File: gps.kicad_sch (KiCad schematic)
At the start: 17 parts, among them J700 Conn_01x02, U700 NEO-6P, X7 Conn_Coaxial

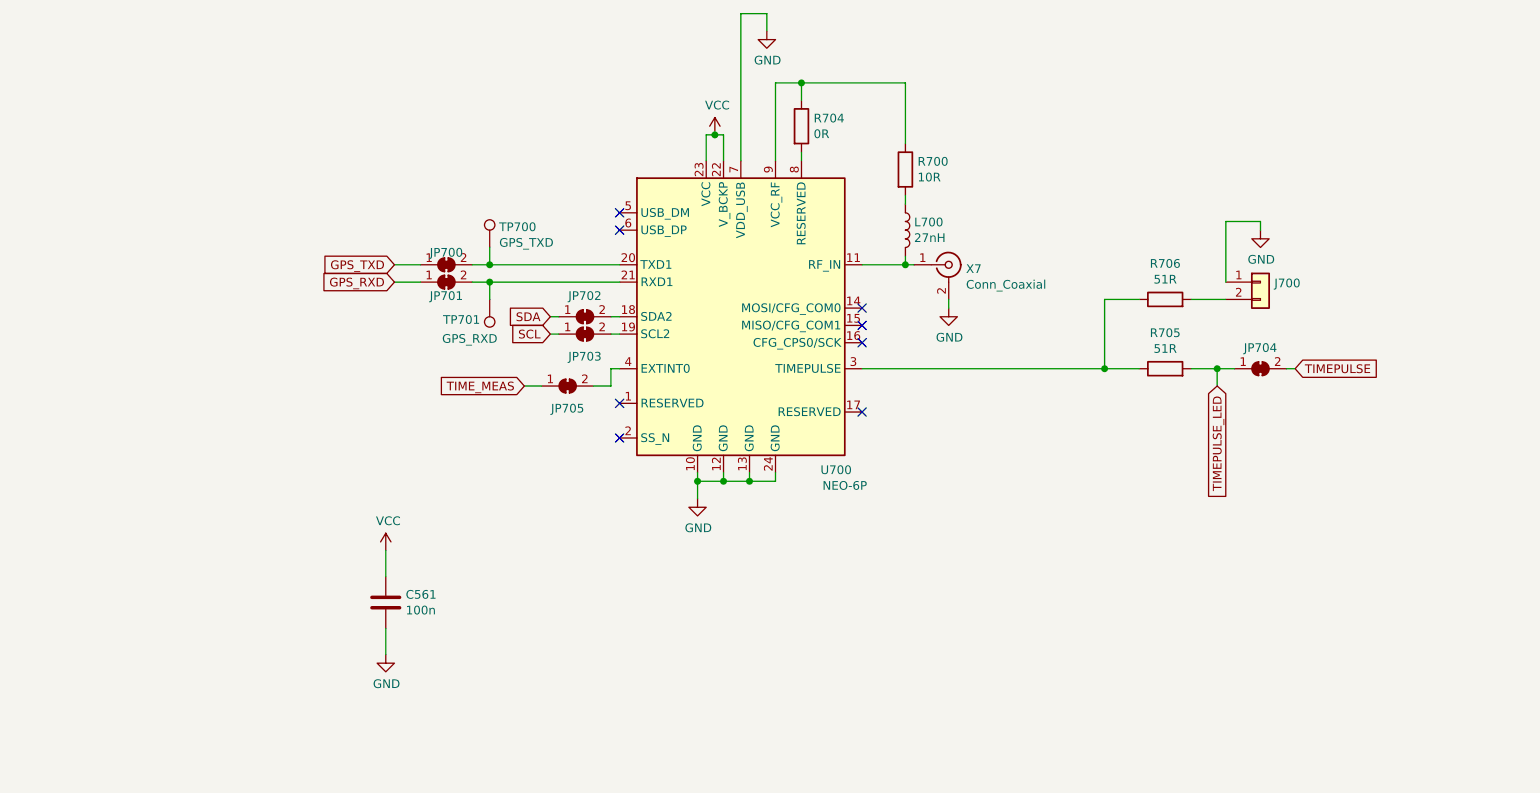
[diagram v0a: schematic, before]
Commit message: Refactored schematic to better show relationship in main schematic
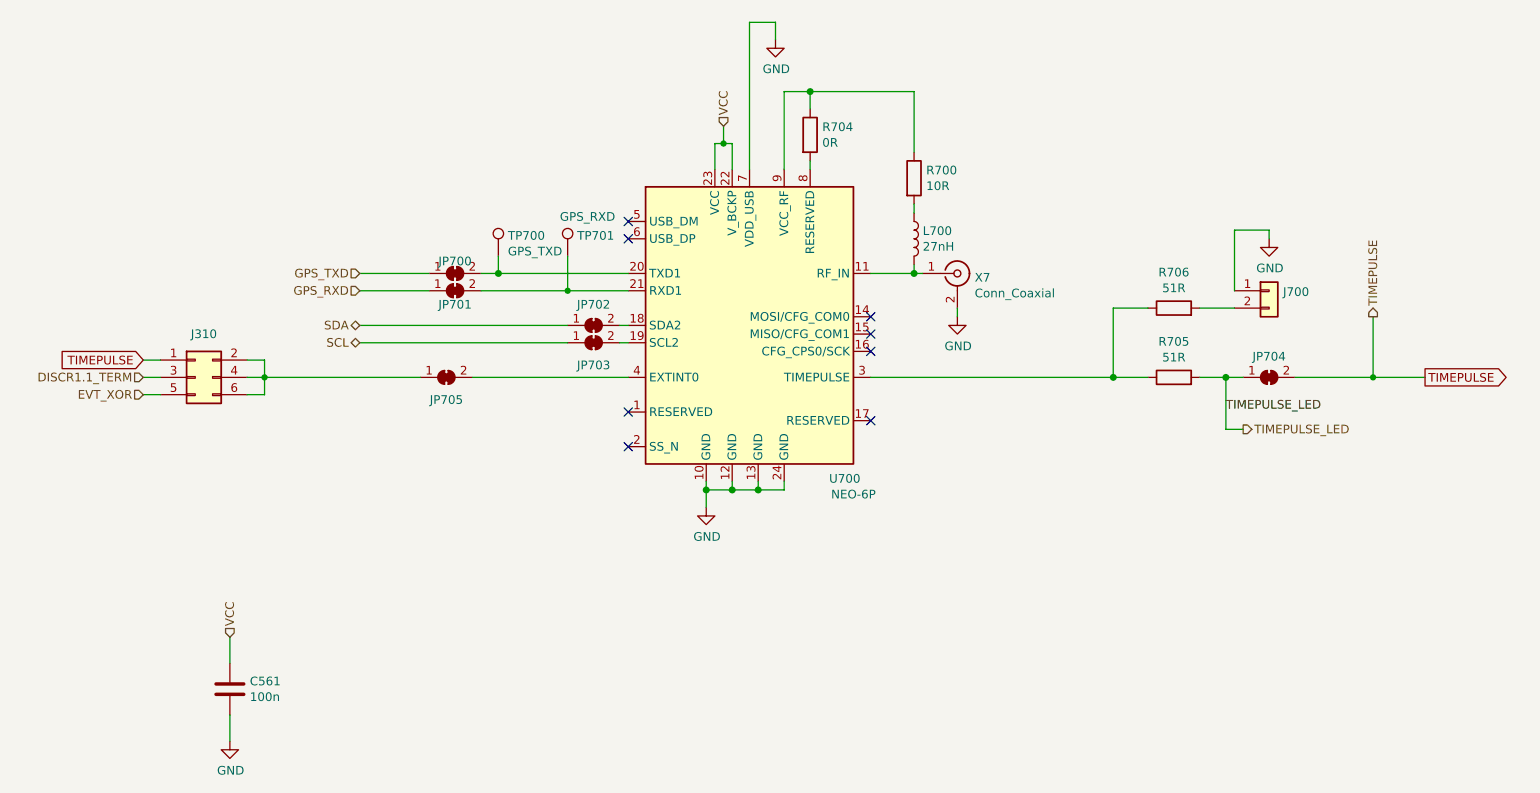
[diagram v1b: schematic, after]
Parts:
- added J310: Conn_02x03_Odd_Even, Connector_PinHeader_2.54mm:PinHeader_2x03_P2.54mm_Vertical, symbol Connector_Generic:Conn_02x03_Odd_Even
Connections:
- net TIMEPULSE: now also J310.1 (Pin_1)
- net TIME_MEAS: no longer names the net of JP705.1 (A)
- net TIME_MEAS: now also J310.2 (Pin_2), J310.4 (Pin_4), J310.6 (Pin_6)
- new net DISCR1.1_TERM: J310.3 (Pin_3)
- new net EVT_XOR: J310.5 (Pin_5)
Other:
- moved on the sheet: C561, J700, JP700, JP701, JP702, JP703, JP704, JP705, L700, R700, R704, R705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

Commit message: Cleaned up board, replaced GPIO footprint with unshrouded version
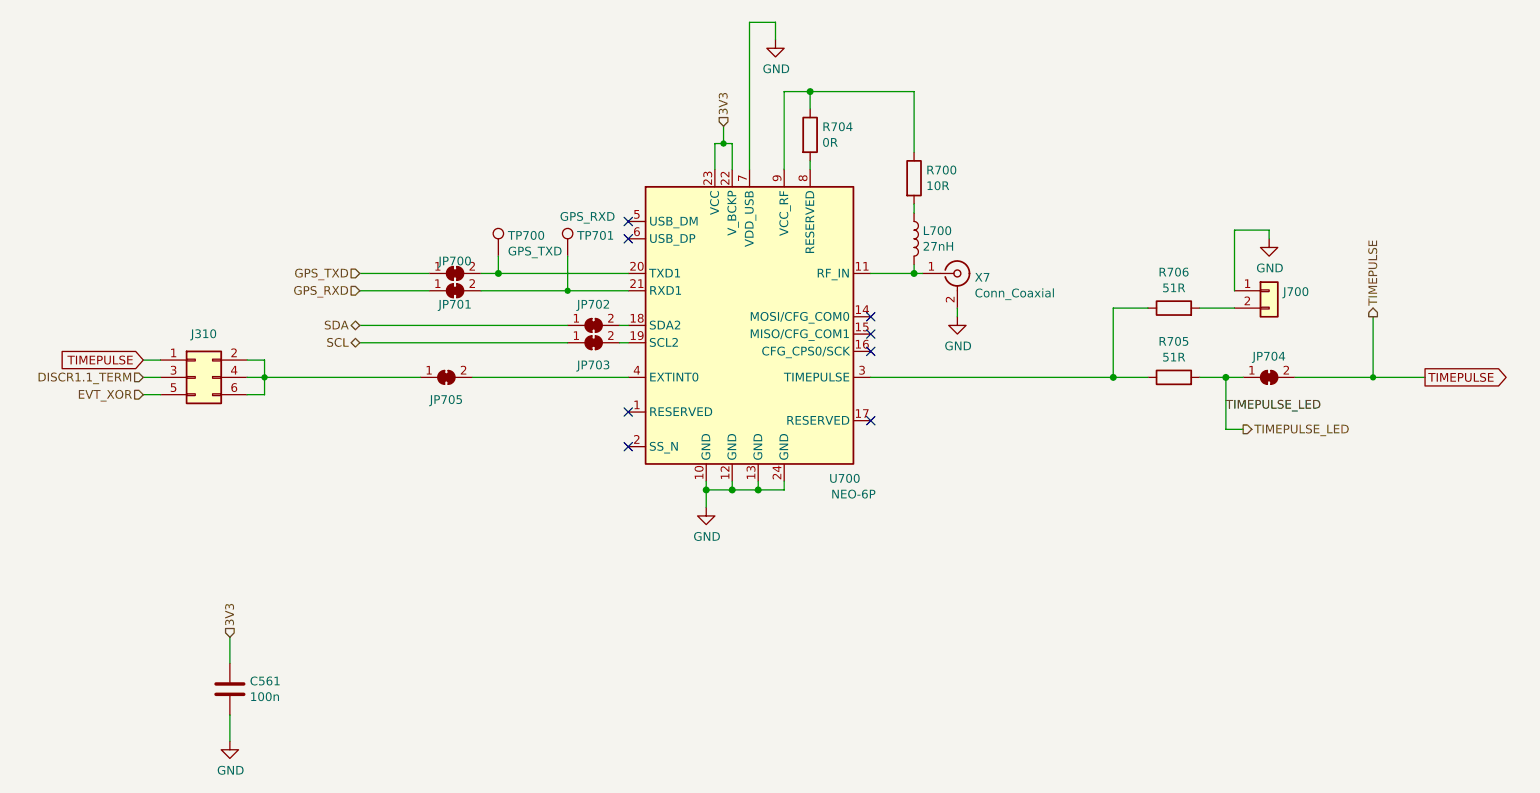
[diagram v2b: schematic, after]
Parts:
- X7: footprint muonpi-kicad-library:Connector_Coaxial_SMA_edge_combined -> muonpi-kicad-library:SMA_Samtec_SMA-J-P-X-ST-EM1_EdgeMount
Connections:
- net VCC renamed 3V3
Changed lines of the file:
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@@
     (effects (font (size 1.27 1.27)) (justify right))
   )
-  (hierarchical_label "VCC" (shape input) (at 71.12 134.62 90)
+  (hierarchical_label "3V3" (shape input) (at 71.12 134.62 90)
     (effects (font (size 1.27 1.27)) (justify left))
   )
@@
     (effects (font (size 1.27 1.27)) (justify right))
   )
-  (hierarchical_label "VCC" (shape input) (at 143.51 59.69 90)
+  (hierarchical_label "3V3" (shape input) (at 143.51 59.69 90)
     (effects (font (size 1.27 1.27)) (justify left))
   )
@@
       (effects (font (size 1.27 1.27)) (justify left))
     )
-    (property "Footprint" "muonpi-kicad-library:Connector_Coaxial_SMA_edge_combined" (id 2) (at 177.8 81.28 0)
-      (effects (font (size 1.27 1.27)) hide)
-    )
+    (property "Footprint" "muonpi-kicad-library:SMA_Samtec_SMA-J-P-X-ST-EM1_EdgeMount" (id 2) (at 177.8 81.28 0)
+      (effects (font (size 1.27 1.27)) hide)
+    )
